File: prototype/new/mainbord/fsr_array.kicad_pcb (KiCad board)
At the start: 4 copper layers, 97.8 x 84.7 mm, 59 parts, among them J1 scanning_ref1, J10 com_adc, J13 com_acc2, J14 com_acc1, J15 com_acc3, J16 com_acc4, J17 usb_B, J2 scanning_ref2, J3 scanning_ref3, J4 scanning_ref4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

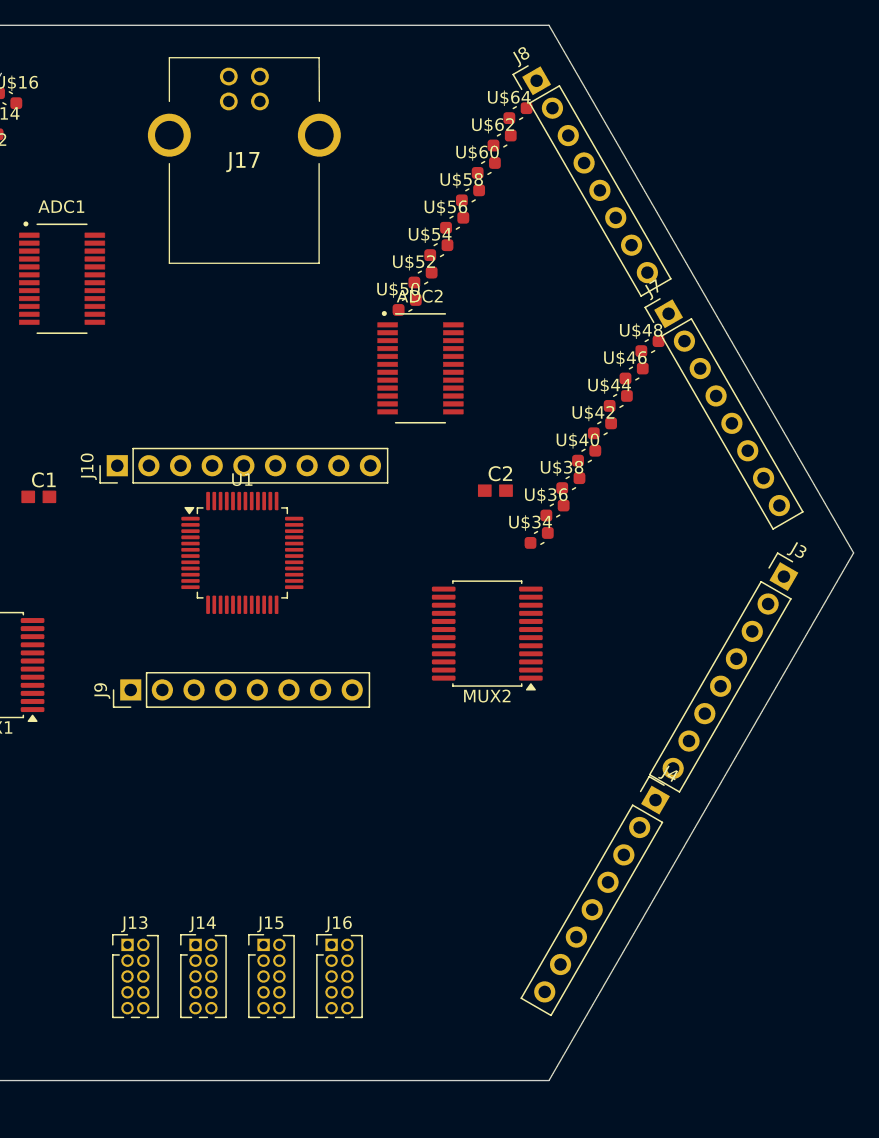
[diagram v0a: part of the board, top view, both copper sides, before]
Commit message: Make hardware PCB layout symmetric
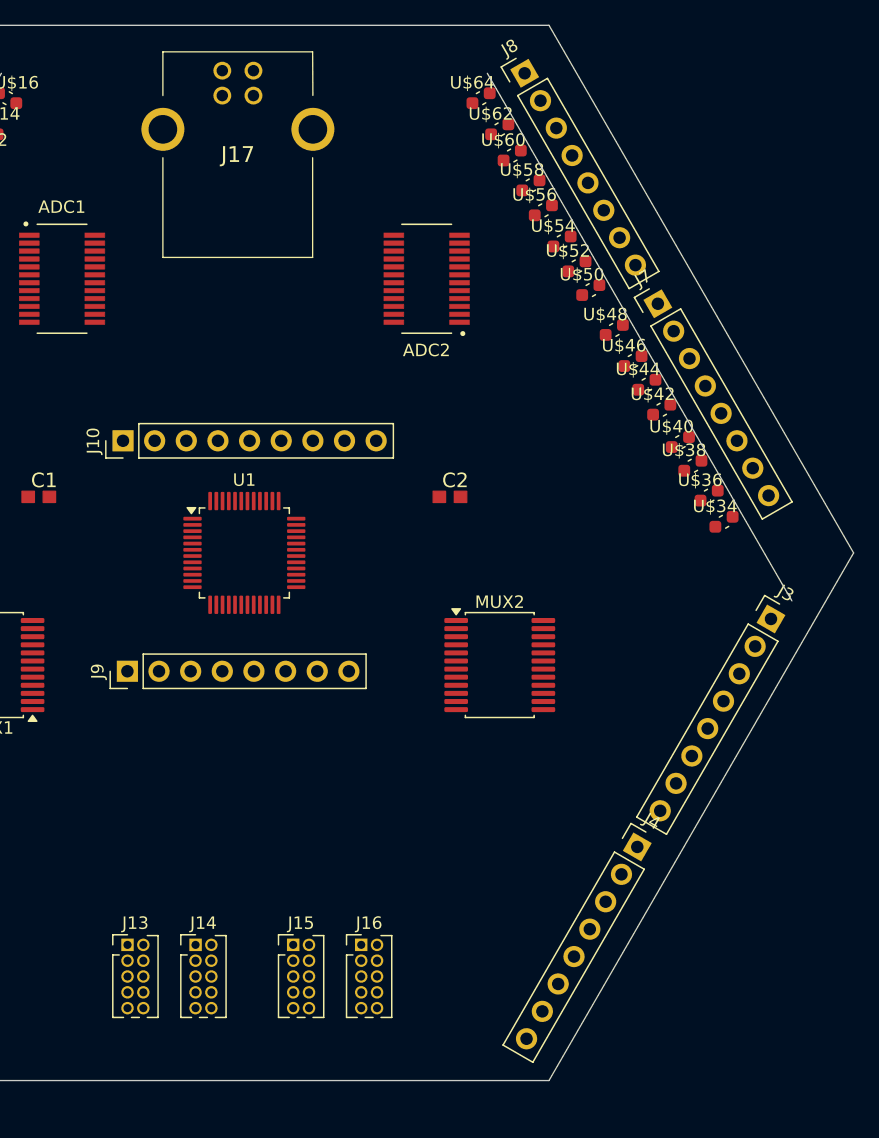
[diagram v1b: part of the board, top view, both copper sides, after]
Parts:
- moved U$34 14.9 mm to (191.5, 93.5)
- moved U$50 14.8 mm to (180.8, 74.9)
- moved U$36 12.4 mm to (190.3, 91.4)
- moved U$52 12.4 mm to (179.7, 73.0)
- moved U$54 9.91 mm to (178.5, 71.0)
- moved U$38 9.89 mm to (189.0, 89.0)
- moved U$40 7.60 mm to (188.0, 87.1)
- moved ADC2 7.21 mm to (167.6, 74.0), turned to 180 degrees
- moved U$56 7.19 mm to (177.0, 68.5)
- moved U$42 4.99 mm to (186.5, 84.5)
- moved U$58 4.92 mm to (176.0, 66.5)
- moved J4 4.03 mm to (184.5, 119.6)
- moved C2 3.68 mm to (169.5, 91.5)
- moved J3 3.55 mm to (195.3, 101.3)
- moved U$64 3.19 mm to (172.0, 59.5)
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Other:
- outline, holes or cut-outs redrawn

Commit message: Compact hardware PCB to 80mm symmetric layout
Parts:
- removed H4, H5: MountingHole, MountingHole:MountingHole_3.2mm_M3
- moved H3 224.2 mm to (166.5, 75.0)
- moved H1 202.0 mm to (153.0, 119.0)
- moved H2 196.0 mm to (139.5, 75.0)
- moved J16 19.0 mm to (161.5, 108.5)
- moved J15 19.0 mm to (155.5, 108.5)
- moved J13 19.0 mm to (143.2, 108.5)
- moved J14 19.0 mm to (149.2, 108.5)
- moved J2 13.4 mm to (133.8, 125.0), turned to 90 degrees
- moved J4 13.4 mm to (172.2, 125.0), turned to -90 degrees
- moved ADC1 10.8 mm to (135.0, 84.2), turned to -30 degrees
- moved ADC2 10.8 mm to (171.0, 84.2), turned to 30 degrees
- moved J3 9.96 mm to (185.3, 101.4)
- moved J1 9.96 mm to (120.7, 101.4)
- moved J5 8.12 mm to (134.6, 64.5)
- moved J8 8.12 mm to (171.4, 64.5)
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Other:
- board size 97.8 x 84.7 mm -> 80 x 69.3 mm
